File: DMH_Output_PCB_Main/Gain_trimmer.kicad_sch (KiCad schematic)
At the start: 10 parts, among them J11 Conn_01x06_PinHeader, J26 Conn_01x06_PinHeader, U8 TL074

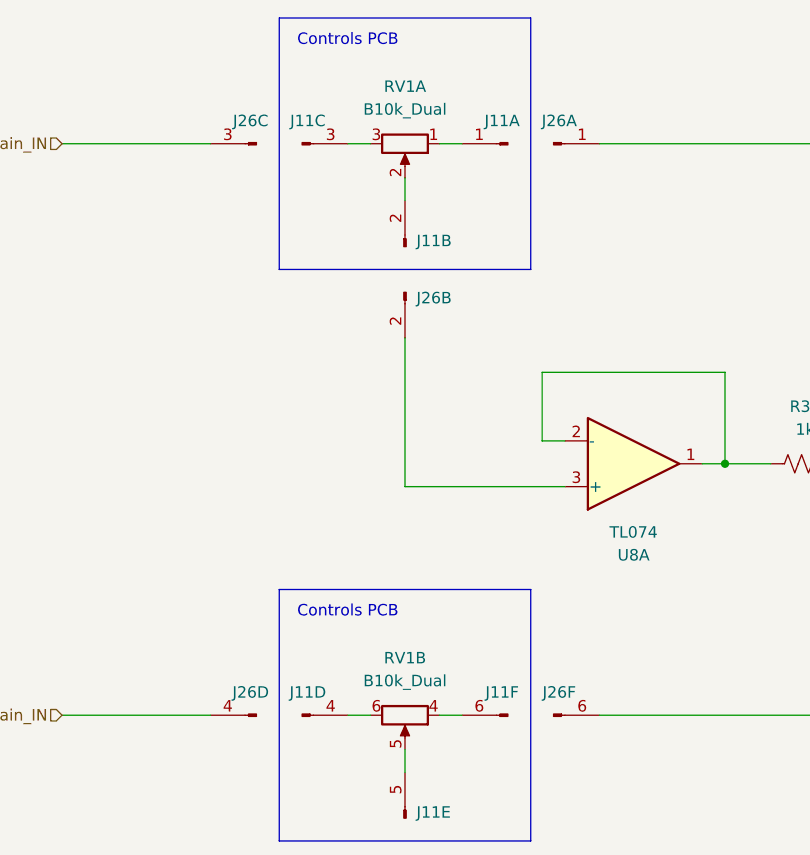
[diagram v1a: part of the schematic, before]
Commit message: Replaced jack symbols with 5pin ones
Also updated Meter LED current source resistor to 75R
Also increased LED guiding PCB mounting holes to M2.5
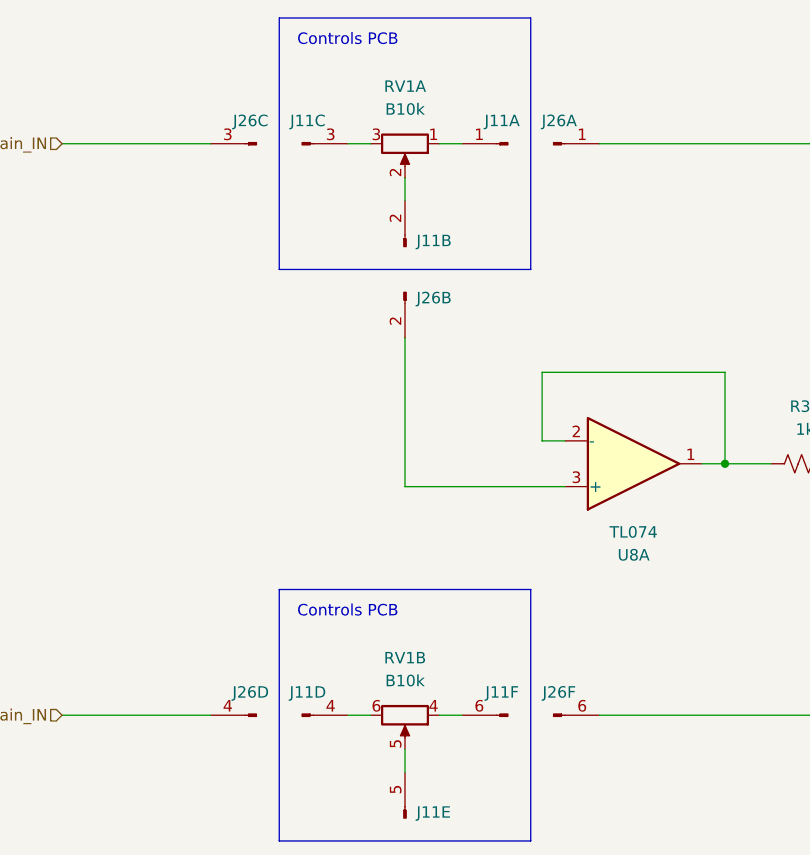
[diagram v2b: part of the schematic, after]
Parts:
- RV1: value B10k_Dual -> B10k; footprint Potentiometer_THT:Potentiometer_Alpha_RD902F-40-00D_Dual_Vertical -> SynthStuff:Potentiometer_Alpha_RD902F-40-00D_Dual_Vertical
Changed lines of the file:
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@@
 			)
 		)
-		(property "Value" "B10k_Dual"
+		(property "Value" "B10k"
 			(at 76.2 46.99 90)
 			(show_name no)
@@
 			)
 		)
-		(property "Footprint" "Potentiometer_THT:Potentiometer_Alpha_RD902F-40-00D_Dual_Vertical"
+		(property "Footprint" "SynthStuff:Potentiometer_Alpha_RD902F-40-00D_Dual_Vertical"
 			(at 76.2 50.8 0)
 			(hide yes)
@@
 					(bold yes)
 					(italic yes)
+				)
+			)
+		)
+		(property "Sim.Library" "${KICAD9_SYMBOL_DIR}/Simulation_SPICE.sp"
+			(at 76.2 50.8 0)
+			(hide yes)
+			(show_name no)
+			(do_not_autoplace no)
+			(effects
+				(font
+					(size 1.27 1.27)
+				)
+			)
+		)
+		(property "Sim.Name" "pot_dual"
+			(at 76.2 50.8 0)
+			(hide yes)
+			(show_name no)
+			(do_not_autoplace no)
+			(effects
+				(font
+					(size 1.27 1.27)
+				)
+			)
+		)
+		(property "Sim.Device" "SUBCKT"
+			(at 76.2 50.8 0)
+			(hide yes)
+			(show_name no)
+			(do_not_autoplace no)
+			(effects
+				(font
+					(size 1.27 1.27)
+				)
+			)
+		)
+		(property "Sim.Pins" "1=r1A 2=wA 3=r0A 4=r1B 5=wB 6=r0B"
+			(at 76.2 50.8 0)
+			(hide yes)
+			(show_name no)
+			(do_not_autoplace no)
+			(effects
+				(font
+					(size 1.27 1.27)
+				)
+			)
+		)
+		(property "Sim.Params" "Rtot=1 wpos=0.4"
+			(at 76.2 50.8 0)
+			(hide yes)
+			(show_name no)
+			(do_not_autoplace no)
+			(effects
+				(font
+					(size 1.27 1.27)
 				)
 			)
@@
 			)
 		)
-		(property "Value" "B10k_Dual"
+		(property "Value" "B10k"
 			(at 76.2 110.49 90)
 			(show_name no)
@@
 			)
 		)
-		(property "Footprint" "Potentiometer_THT:Potentiometer_Alpha_RD902F-40-00D_Dual_Vertical"
+		(property "Footprint" "SynthStuff:Potentiometer_Alpha_RD902F-40-00D_Dual_Vertical"
 			(at 76.2 114.3 0)
 			(hide yes)
@@
 				)
 			)
+		)
+		(property "Sim.Library" "${KICAD9_SYMBOL_DIR}/Simulation_SPICE.sp"
+			(at 76.2 114.3 0)
+			(hide yes)
+			(show_name no)
+			(do_not_autoplace no)
+			(effects
+				(font
+					(size 1.27 1.27)
+				)
+			)
+		)
+		(property "Sim.Name" "pot_dual"
+			(at 76.2 114.3 0)
+			(hide yes)
+			(show_name no)
+			(do_not_autoplace no)
+			(effects
+				(font
+					(size 1.27 1.27)
+				)
+			)
+		)
+		(property "Sim.Device" "SUBCKT"
+			(at 76.2 114.3 0)
+			(hide yes)
+			(show_name no)
+			(do_not_autoplace no)
+			(effects
+				(font
+					(size 1.27 1.27)
+				)
+			)
+		)
+		(property "Sim.Pins" "1=r1A 2=wA 3=r0A 4=r1B 5=wB 6=r0B"
+			(at 76.2 114.3 0)
+			(hide yes)
+			(show_name no)
+			(do_not_autoplace no)
+			(effects
+				(font
+					(size 1.27 1.27)
+				)
+			)
+		)
+		(property "Sim.Params" "Rtot=1 wpos=0.4"
+			(at 76.2 114.3 0)
+			(hide yes)
+			(show_name no)
+			(do_not_autoplace no)
+			(effects
+				(font
+					(size 1.27 1.27)
+				)
+			)

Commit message: Prep for Main and MZ PCBs design in progress
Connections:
- net L_Gain_IN renamed L_Gain_IN_M
- net L_Gain_OUT renamed L_Gain_OUT_M
- net R_Gain_IN renamed R_Gain_IN_M
- net R_Gain_OUT renamed R_Gain_OUT_M
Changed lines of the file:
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@@
 		)
 	)
-	(hierarchical_label "L_Gain_OUT"
+	(hierarchical_label "L_Gain_OUT_M"
 		(shape output)
 		(at 154.94 88.9 0)
@@
 		)
 	)
-	(hierarchical_label "L_Gain_IN"
+	(hierarchical_label "L_Gain_IN_M"
 		(shape input)
 		(at 38.1 50.8 180)
@@
 		)
 	)
-	(hierarchical_label "R_Gain_OUT"
+	(hierarchical_label "R_Gain_OUT_M"
 		(shape output)
 		(at 154.94 152.4 0)
@@
 		)
 	)
-	(hierarchical_label "R_Gain_IN"
+	(hierarchical_label "R_Gain_IN_M"
 		(shape input)
 		(at 38.1 114.3 180)
